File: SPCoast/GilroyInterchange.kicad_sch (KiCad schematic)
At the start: 74 parts, among them SW5777 777, SW5781 781

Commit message: feat(kicad): owner edit (2026-10-25): Milepost carries Name = ${Value}; mileposts ground the region at Lick
The Milepost symbol gains Name = ${Value} like every other keyed symbol, so the
compiler reads no Value for it. The two Luchessa mileposts take the field, and
three new mileposts are placed: 55.3 (Lick) and 77.1 at Gilroy Caltrain, 77.0 at
Gilroy Interchange. Panels/ is left untracked.

Verified: lint_symbol_fields 100 symbols, 0 errors, 0 warnings; the diff is
additions only, no instance field reset; FieldUnit-Subdivision 201 tests against
a fresh export; compile_layout.py --geometry writes mileposts 55.3, 77.1, 77.0,
78.3, 79.3 with no geometry info.

Co-Authored-By: Claude Fable 5.1 <noreply@anthropic.com>
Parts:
- added MP7005: 77.0, symbol Railroad-Trackplan:Milepost
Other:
- note added: "Rucker"
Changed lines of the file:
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@@
+		)
+	)
+	(text "Rucker"
+		(exclude_from_sim no)
+		(at 75.184 61.722 0)
+		(effects
+			(font
+				(size 1.27 1.27)
+			)
 		)
 	)
@@
 					(unit 1)
 				)
+			)
+		)
+	)
+	(symbol
+		(lib_id "Railroad-Trackplan:Milepost")
+		(at 63.5 59.69 0)
+		(unit 1)
+		(body_style 1)
+		(exclude_from_sim no)
+		(in_bom yes)
+		(on_board yes)
+		(in_pos_files yes)
+		(dnp no)
+		(property "Reference" "MP7005"
+			(at 59.69 56.515 0)
+			(hide yes)
+			(show_name no)
+			(do_not_autoplace no)
+			(effects
+				(font
+					(size 1.27 1.27)
+				)
+				(justify left)
+			)
+		)
+		(property "Value" "77.0"
+			(at 63.5 52.705 0)
+			(show_name no)
+			(do_not_autoplace yes)
+			(effects
+				(font
+					(size 1.27 1.27)
+				)
+			)
+		)
+		(property "Footprint" ""
+			(at 63.5 59.69 0)
+			(hide yes)
+			(show_name no)
+			(do_not_autoplace no)
+			(effects
+				(font
+					(size 1.27 1.27)
+				)
+			)
+		)
+		(property "Datasheet" ""
+			(at 63.5 59.69 0)
+			(hide yes)
+			(show_name no)
+			(do_not_autoplace no)
+			(effects
+				(font
+					(size 1.27 1.27)
+				)
+			)
+		)
+		(property "Description" "Milepost: a track anchor carrying the milepost of the point it sits on."
+			(at 63.5 59.69 0)
+			(hide yes)
+			(show_name no)
+			(do_not_autoplace no)
+			(effects
+				(font
+					(size 1.27 1.27)
+				)
+			)
+		)
+		(property "Role" "TRACK"
+			(at 63.5 59.69 0)
+			(hide yes)
+			(show_name no)
+			(do_not_autoplace no)
+			(effects
+				(font
+					(size 1.27 1.27)
+				)
+			)
+		)
+		(property "Kind" "MILEPOST"
+			(at 63.5 59.69 0)
+			(hide yes)
+			(show_name no)
+			(do_not_autoplace no)
+			(effects
+				(font
+					(size 1.27 1.27)
+				)
+			)
+		)
+		(property "Name" "${Value}"
+			(at 63.5 59.69 0)
+			(hide yes)
+			(show_name no)
+			(do_not_autoplace no)
+			(effects
+				(font
+					(size 1.27 1.27)
+				)
+			)
+		)
+		(instances
+			(project "SPCoast"
+				(path "/528348b2-add8-5367-a5f7-439c76f0ca33/2ed995e3-3819-55cd-b8d9-5c2af048ccb4/defc570c-1f61-4751-be37-2827b304f837"
+					(reference "MP7005")
+					(unit 1)
+				)

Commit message: feat(kicad): owner edit (2026-10-26): NextCP carries Interlocking; Industry carries Name; HBA leaves the track
The owner's edits after the trackplan review:
- NextCP gains Interlocking = ${Value}, a key the compiler reads for the destination; every instance takes it.
  Christopher's two NextCPs toward Corporal now say Corporal (both said Sargent).
- Industry gains Name = ${VALUE}. The five Industries are named: Gilroy Industry at Luchessa, Beet Loader 1
  and 2 at Corporal and at Sargent.
- Sargent's HBA (hot box alarm) is moved off 1SAT's net; its MC pin is unconnected and it carries Milepost 83.4.
- Watsonville: one Rule 93 (YARD) symbol is moved to the yard side of its joint.
Panels/ is left untracked.

Verified:
- Netlist exported by the owner 2026-10-26 12:37, newer than every sheet and the library.
- lint_symbol_fields: 100 symbols, 0 errors, 0 warnings.

Co-Authored-By: Claude Opus 5.5 <noreply@anthropic.com>
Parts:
- CP5001, CP5002: Interlocking (none) -> ${Value}
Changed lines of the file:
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@@
 		)
 		(property "Value" "Luchessa"
-			(at 194.945 77.47 0)
-			(show_name no)
-			(do_not_autoplace no)
+			(at 199.39 86.36 0)
+			(hide yes)
+			(show_name no)
+			(do_not_autoplace yes)
 			(effects
 				(font
@@
 		(property "Kind" "NEXT_CP"
 			(at 196.85 77.47 0)
+			(hide yes)
+			(show_name no)
+			(do_not_autoplace no)
+			(effects
+				(font
+					(size 1.27 1.27)
+				)
+			)
+		)
+		(property "Interlocking" "${Value}"
+			(at 199.39 86.36 0)
 			(hide yes)
 			(show_name no)
@@
 		)
 		(property "Value" "Gilroy Caltrain"
-			(at 51.435 77.47 0)
-			(show_name no)
-			(do_not_autoplace no)
+			(at 55.88 86.36 0)
+			(hide yes)
+			(show_name no)
+			(do_not_autoplace yes)
 			(effects
 				(font
@@
 			(hide yes)
 			(show_name no)
+			(do_not_autoplace no)
+			(effects
+				(font
+					(size 1.27 1.27)
+				)
+			)
+		)
+		(property "Interlocking" "${Value}"
+			(at 55.88 86.36 0)
+			(hide yes)
+			(show_name no)

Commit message: refactor(symbols): the CP field is CP Name on every trackplan symbol
One fact, which house an appliance or circuit stands in, had two field
names: CP Name on the House and PanelColumn, CP on 17 trackplan
symbols. Every CP is now CP Name, in the library and in each placed
symbol, by a text rename of the field name only (KiCad's update
symbols was not used; it resets per-instance fields).

Verified: fresh kicad-cli netlists before and after: 754 components on
both, 136 had CP, every field identical once CP is read as CP Name, no
CP left. lint_symbol_fields: 100 symbols, 0 errors, 0 warnings.

Co-Authored-By: Claude Opus 5.5 <noreply@anthropic.com>
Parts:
- B5001, B5007, SW5777, TC5001, TC5002, TC5003, TC5004: CP Gilroy North -> (none); CP Name (none) -> Gilroy North
- B5002, B5008, SW5781: CP Gilroy South -> (none); CP Name (none) -> Gilroy South
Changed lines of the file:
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@@
 			)
 		)
-		(property "CP" "Gilroy North"
+		(property "CP Name" "Gilroy North"
 			(at 74.93 74.93 0)
 			(show_name no)
@@
 			)
 		)
-		(property "CP" "Gilroy North"
+		(property "CP Name" "Gilroy North"
 			(at 106.68 63.5 0)
 			(show_name no)
@@
 			)
 		)
-		(property "CP" "Gilroy North"
+		(property "CP Name" "Gilroy North"
 			(at 63.5 79.375 0)
 			(show_name no)
@@
 			)
 		)
-		(property "CP" "Gilroy South"
+		(property "CP Name" "Gilroy South"
 			(at 156.21 81.915 0)
 			(show_name no)
@@
 			)
 		)
-		(property "CP" "Gilroy North"
+		(property "CP Name" "Gilroy North"
 			(at 87.63 81.915 0)
 			(show_name no)
@@
 			)
 		)
-		(property "CP" "Gilroy North"
+		(property "CP Name" "Gilroy North"
 			(at 120.65 65.024 0)
 			(show_name no)
@@
 			)
 		)
-		(property "CP" "Gilroy South"
+		(property "CP Name" "Gilroy South"
 			(at 168.91 80.01 0)
 			(show_name no)
@@
 			)
 		)
-		(property "CP" "Gilroy North"
+		(property "CP Name" "Gilroy North"
 			(at 182.88 79.375 0)
 			(show_name no)
@@
 			)
 		)
-		(property "CP" "Gilroy South"
+		(property "CP Name" "Gilroy South"
 			(at 137.16 58.42 0)
 			(show_name no)
@@
 			)
 		)
-		(property "CP" "Gilroy North"
+		(property "CP Name" "Gilroy North"
 			(at 120.65 79.375 0)
 			(show_name no)

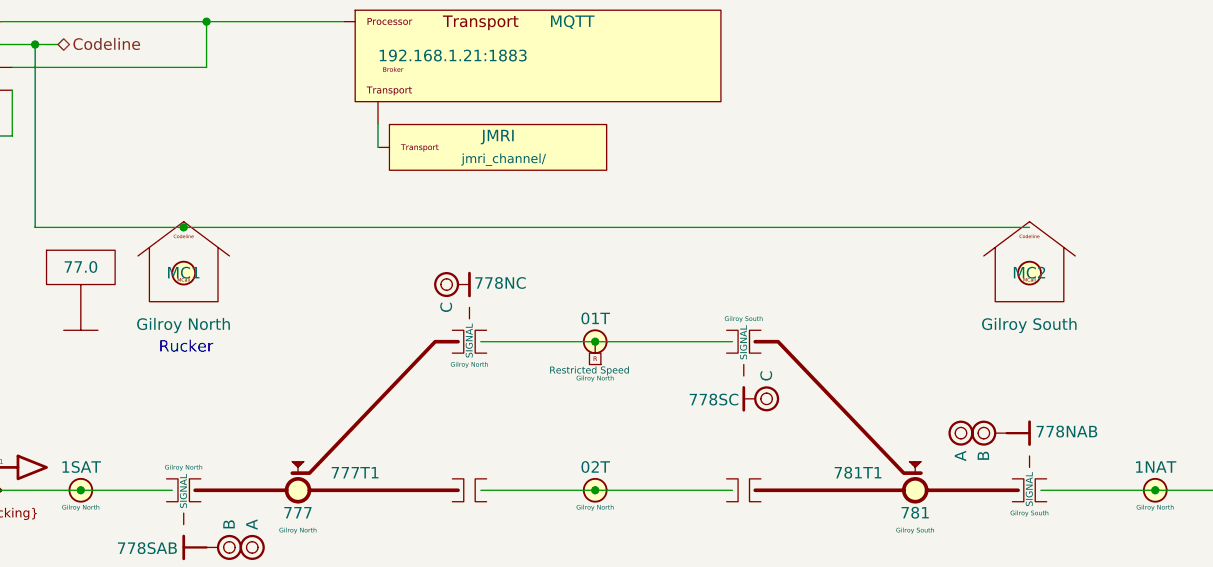
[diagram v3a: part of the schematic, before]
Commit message: feat(symbols): maintainer call as one two-unit symbol, named 1MC, proven on Gilroy Interchange
The owner's proof of concept in KiCad. PanelMCall is one symbol with a
lever unit (MCS) and a lamp unit (MCK), Name=${Value}MC (AAR style 3,
a number prefix), and Control=${Name}S, Indication=${Name}K stating
its tokens. The trackplan MaintainerCall takes Name=${Value}MC and
Indication=${Name}K. Gilroy Interchange's two calls are redrawn: 1MC
in Gilroy North and column 3, 2MC in Gilroy South and column 4.
Gilroy Caltrain only refreshes its cached Milepost symbol.

Verified: fresh compile places 1MC and 2MC in their houses and
columns, bindings on 0x22 and 0x23. Expected and pending: two
reference.unresolved (the importer still builds Name + pin, 1MCMCK)
and three lint errors (the lint does not yet know Control and
Indication); both are the importer and lint side of the change.

Co-Authored-By: Claude Opus 5.5 <noreply@anthropic.com>
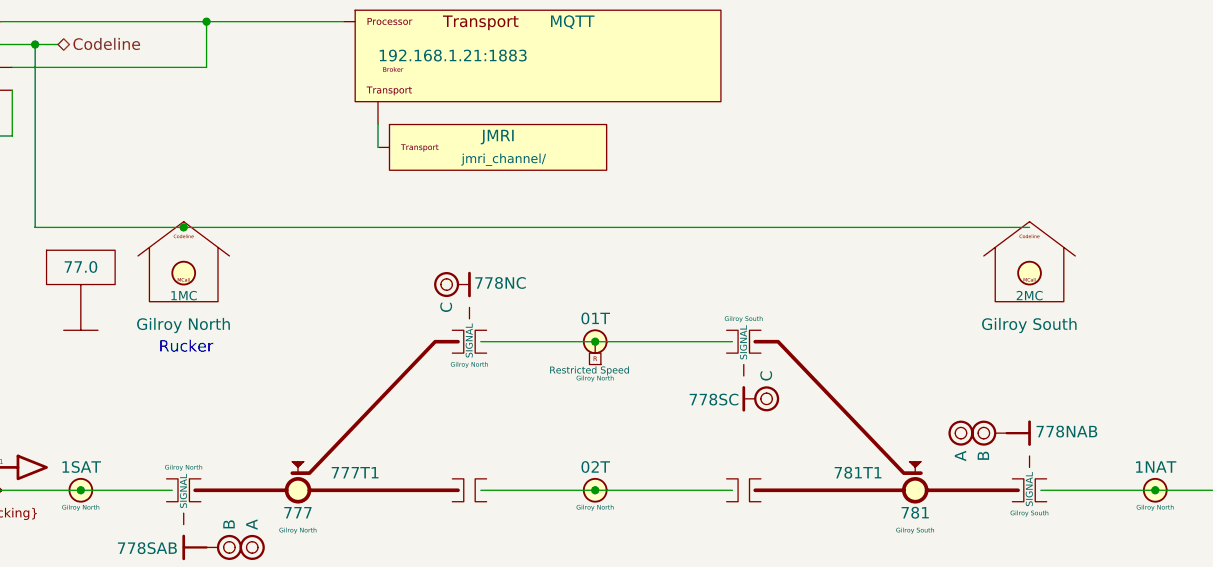
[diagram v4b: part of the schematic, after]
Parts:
- MC5001: value MC1 -> 1; Indication (none) -> ${Name}K; Name ${Value} -> ${Value}MC
- MC5002: value MC2 -> 2; Indication (none) -> ${Name}K; Name ${Value} -> ${Value}MC
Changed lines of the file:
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@@
 			)
 		)
-		(property "Value" "MC2"
+		(property "Value" "2"
 			(at 168.91 53.34 0)
+			(hide yes)
 			(show_name no)
 			(do_not_autoplace no)
@@
 			)
 		)
-		(property "Name" "${Value}"
-			(at 168.91 53.34 0)
-			(hide yes)
+		(property "Name" "${Value}MC"
+			(at 168.91 55.88 0)
 			(show_name no)
-			(do_not_autoplace no)
+			(do_not_autoplace yes)
 			(effects
 				(font
-					(size 1.27 1.27)
+					(size 1.016 1.016)
 				)
 			)
@@
 			)
 		)
+		(property "Indication" "${Name}K"
+			(at 173.99 53.34 0)
+			(hide yes)
+			(show_name no)
+			(do_not_autoplace no)
+			(effects
+				(font
+					(size 1.27 1.27)
+				)
+			)
+		)
 		(pin "1"
 		)
@@
 	)
 	(symbol
+		(lib_name "MaintainerCall_1")
 		(lib_id "Railroad-Trackplan:MaintainerCall")
 		(at 74.93 53.34 0)
@@
 			)
 		)
-		(property "Value" "MC1"
+		(property "Value" "1"
 			(at 74.93 53.34 0)
+			(hide yes)
 			(show_name no)
 			(do_not_autoplace no)
@@
 			)
 		)
-		(property "Name" "${Value}"
-			(at 74.93 53.34 0)
-			(hide yes)
+		(property "Name" "${Value}MC"
+			(at 74.93 55.88 0)
 			(show_name no)
-			(do_not_autoplace no)
+			(do_not_autoplace yes)
 			(effects
 				(font
-					(size 1.27 1.27)
+					(size 1.016 1.016)
 				)
 			)
@@
 			(hide yes)
 			(show_name no)
+			(do_not_autoplace no)
+			(effects
+				(font
+					(size 1.27 1.27)
+				)
+			)
+		)
+		(property "Indication" "${Name}K"
+			(at 80.01 53.34 0)
+			(hide yes)
+			(show_name no)

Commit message: feat(spcoast): per-pin token fields on the panels, lamp Indication expressions, maintainer calls named 1MC
Applies the symbol rulings of 2026-10-28 to every sheet: the lib_symbols
caches of the changed symbols are the library's copies (this also clears
the stale PanelMCall and MaintainerCall caches), and every placed
instance gets the new hidden Control.*/Indication.* fields, loses
PanelLock Invert, and PanelMCall's whole-symbol Control and Indication
(Pin.MCK binary). Model lamps' IndicationToken becomes Indication: each
comma-separated circuit gets its K, qualifiers kept, joined with " | "
(795T1,01T,799T1 -> 795T1K | 01TK | 799T1K).

Maintainer calls in Christopher (1, 2), Corporal, Luchessa and Sargent
follow Gilroy Interchange (5dad54f): Value MC<n> -> <n>, Name ${Value}MC,
and the separate PanelMCall-Lamp is replaced by unit 2 of the same
PanelMCall at the old lamp's position, so its MCK pin sits where the
LAMP pin was. The old lamps' Column pin touched PanelColumn pin 8
directly (no wire); that pin is now unconnected, as on Gilroy
Interchange. Gilroy Interchange's local MaintainerCall_1 cache and its
two trackplan calls lose Indication.

Verified: fresh netlist before/after: components 752 -> 747 (the five
lamps), nets 1028 -> 1028; each old LAMP-pin net now holds the lever's
unit-2 MCK pin (pin 3) on the same expander pin (B1, pin 9); the levers'
nets are renamed only (~{S} -> ~{MCS}, unit suffix A); no other net
changed. Every field difference is an intended one. ERC 18 -> 1
violations (lib_symbol_mismatch 17 -> 0; pre-existing Sargent AUX1
pin_not_connected remains).

Co-Authored-By: Claude Opus 5.5 <noreply@anthropic.com>
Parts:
- MC5001, MC5002: Indication ${Name}K -> (none)
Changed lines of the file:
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@@
 			)
 		)
-		(property "Indication" "${Name}K"
-			(at 173.99 53.34 0)
-			(hide yes)
-			(show_name no)
-			(do_not_autoplace no)
-			(effects
-				(font
-					(size 1.27 1.27)
-				)
-			)
-		)
 		(pin "1"
 		)
@@
 			(hide yes)
 			(show_name no)
-			(do_not_autoplace no)
-			(effects
-				(font
-					(size 1.27 1.27)
-				)
-			)
-		)
-		(property "Indication" "${Name}K"
-			(at 80.01 53.34 0)
-			(hide yes)
-			(show_name no)

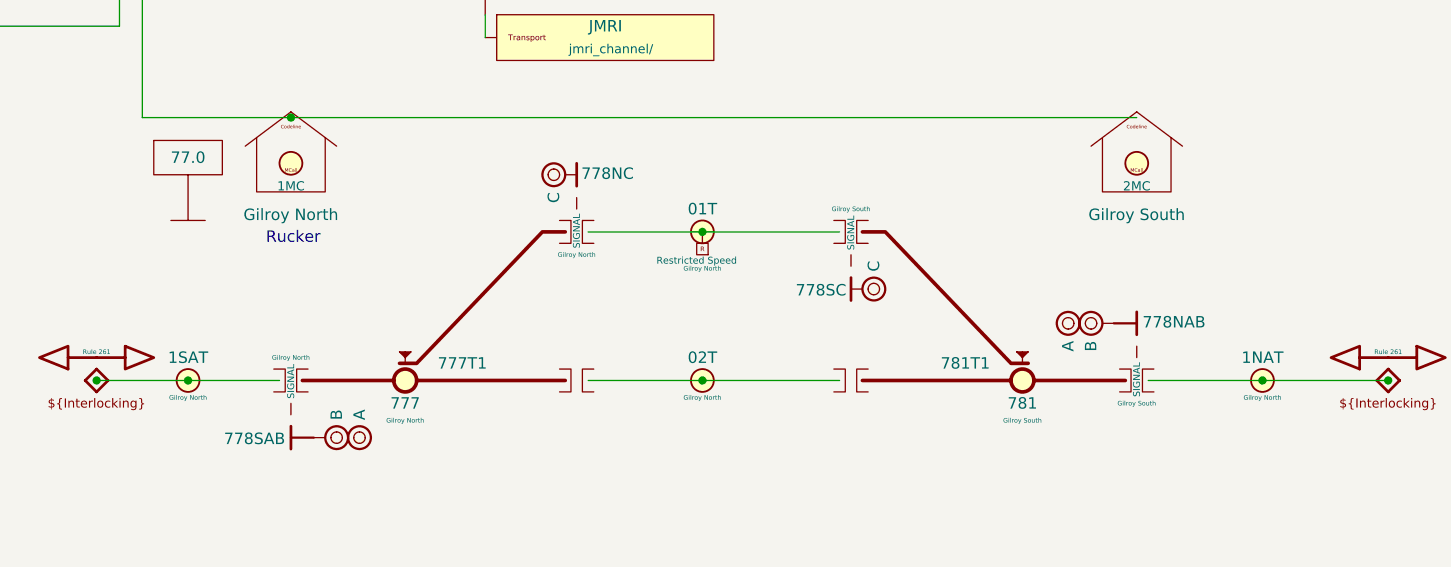
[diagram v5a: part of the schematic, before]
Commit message: feat(symbols,spcoast): track circuits state their Indication; virtual circuits list Members
The owner's edit, 2026-10-29. Every Track Circuit symbol (plain, RED,
Yellow, Virtual) carries Indication=${Name}K: the token a local circuit
reports and a remote consumer (Sargent's Corporal:2NAT) consumes, so
both sides state it and match token to token. Track Circuit_Virtual's
IndicationToken becomes Members (the local circuits it is made of, not
tokens), with Display=${Value}: [${Members}]. Sargent's HBA gets a
no-connect on its unused pin. The panel sheets are re-saved by KiCad
with no field changes.

Verified:
- netlist field diff against 69e87ec: 747 components, none added or
  removed; the only changes are Indication added on 63 track circuits
  (26 Track Circuit, 35 Yellow, 2 Virtual) and IndicationToken renamed
  to Members on TC15032 and TC15034
- ERC: 0 violations (was 1, Sargent AUX1 pin_not_connected)
- Subdivision lint_symbol_fields: 100 symbols, 0 errors, 0 warnings
- Subdivision fresh compile: 0 errors, 0 warnings, 8 info, 2 missing;
  consumer.legacy_token no longer fires

Co-Authored-By: Claude Opus 5.5 <noreply@anthropic.com>
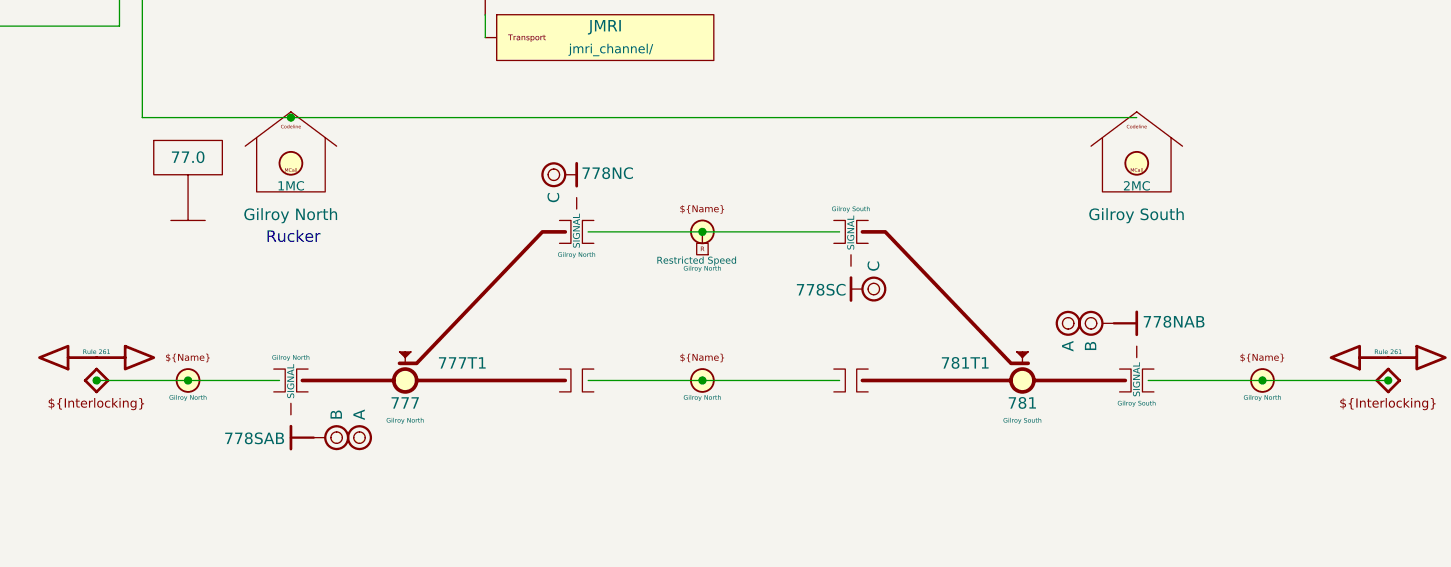
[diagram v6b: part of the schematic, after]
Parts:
- TC5001, TC5002, TC5003, TC5004: Indication (none) -> ${Name}K
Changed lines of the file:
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@@
 		)
 		(property "Value" "1SAT"
-			(at 63.5 74.93 0)
+			(at 63.5 80.01 0)
+			(hide yes)
 			(show_name no)
-			(do_not_autoplace no)
+			(do_not_autoplace yes)
 			(effects
 				(font
@@
 			)
 		)
+		(property "Indication" "${Name}K"
+			(at 64.77 83.82 0)
+			(hide yes)
+			(show_name no)
+			(do_not_autoplace no)
+			(effects
+				(font
+					(size 1.27 1.27)
+				)
+			)
+		)
 		(pin "1"
 		)
@@
 		)
 		(property "Value" "01T"
-			(at 120.65 58.42 0)
+			(at 120.65 63.5 0)
+			(hide yes)
 			(show_name no)
-			(do_not_autoplace no)
+			(do_not_autoplace yes)
 			(effects
 				(font
@@
 			)
 		)
+		(property "Indication" "${Name}K"
+			(at 121.92 67.31 0)
+			(hide yes)
+			(show_name no)
+			(do_not_autoplace no)
+			(effects
+				(font
+					(size 1.27 1.27)
+				)
+			)
+		)
 		(pin "1"
 		)
@@
 		)
 		(property "Value" "1NAT"
-			(at 182.88 74.93 0)
+			(at 182.88 80.01 0)
+			(hide yes)
 			(show_name no)
-			(do_not_autoplace no)
+			(do_not_autoplace yes)
 			(effects
 				(font
@@
 			)
 		)
+		(property "Indication" "${Name}K"
+			(at 184.15 83.82 0)
+			(hide yes)
+			(show_name no)
+			(do_not_autoplace no)
+			(effects
+				(font
+					(size 1.27 1.27)
+				)
+			)
+		)
 		(pin "1"
 		)
@@
 		)
 		(property "Value" "02T"
-			(at 120.65 74.93 0)
+			(at 120.65 80.01 0)
+			(hide yes)
 			(show_name no)
-			(do_not_autoplace no)
+			(do_not_autoplace yes)
 			(effects
 				(font
@@
 			(hide yes)
 			(show_name no)
+			(do_not_autoplace no)
+			(effects
+				(font
+					(size 1.27 1.27)
+				)
+			)
+		)
+		(property "Indication" "${Name}K"
+			(at 121.92 83.82 0)
+			(hide yes)
+			(show_name no)

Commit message: feat(symbols): switches and field lamps state their indication token
A switch states its OS circuit's token, Indication=${TC}K, on Switch_Dual,
Switch_Lock, Switch_Powered, Switch_Powered_Diag, Switch_Powered_Small and
Derail_TC; symbols with no TC (Derail, Switch_Manual, Switch_Manual_Sensed,
Switch_Powered_NO_TC) carry the field present and empty. The AUXILIARY field
lamp states Indication=${Name}K. The four NFLK/SFLK lamps in Luchessa and
Watsonville are renamed NFL/SFL, so their tokens stay NFLK/SFLK. The
sheets are updated from the library.

Verified:
- fresh kicad-cli netlist vs HEAD 6ce30b3: 747 components each, 46 field
  changes: 31 switch/derail Indication, HBA Indication=HBAK, the four
  NFL/SFL renames with their Indication, and MC5001's library entry name
  (MaintainerCall_1 -> MaintainerCall); nothing else
- kicad-cli ERC: 0 violations
- tools/contract/lint_symbol_fields.py: 100 symbols, 0 errors, 0 warnings
- compile_layout.py: 0 errors, 0 warnings, 8 info, 2 missing (unchanged)

Co-Authored-By: Claude Opus 5.5 <noreply@anthropic.com>
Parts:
- SW5777, SW5781: Indication (none) -> ${TC}K
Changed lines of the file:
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@@
 			)
 		)
+		(property "Indication" "${TC}K"
+			(at 156.21 77.47 0)
+			(hide yes)
+			(show_name no)
+			(do_not_autoplace no)
+			(effects
+				(font
+					(size 1.27 1.27)
+				)
+			)
+		)
 		(pin "3"
 		)
@@
 			)
 		)
+		(property "Indication" "${TC}K"
+			(at 87.63 77.47 0)
+			(hide yes)
+			(show_name no)
+			(do_not_autoplace no)
+			(effects
+				(font
+					(size 1.27 1.27)
+				)
+			)
+		)
 		(pin "3"
 		)
@@
 	)
 	(symbol
-		(lib_name "MaintainerCall_1")
 		(lib_id "Railroad-Trackplan:MaintainerCall")
 		(at 74.93 53.34 0)
